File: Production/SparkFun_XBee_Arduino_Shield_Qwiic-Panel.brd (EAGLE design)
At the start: 120.9 x 213.4 mm, 1008 parts, among them J1 QWIIC_RIGHT_ANGLE, J13 QWIIC_RIGHT_ANGLE, J17 QWIIC_RIGHT_ANGLE, J21 QWIIC_RIGHT_ANGLE, J4 QWIIC_RIGHT_ANGLE, J9 QWIIC_RIGHT_ANGLE, Q1 220mA/50V/3.5Ω, Q11 3.1A/30V/105mΩ, Q12 220mA/50V/3.5Ω, Q13 20V/4.2A/52mΩ/1.4W, Q15 3.1A/30V/105mΩ, Q16 220mA/50V/3.5Ω, Q17 20V/4.2A/52mΩ/1.4W, Q19 3.1A/30V/105mΩ, Q2 20V/4.2A/52mΩ/1.4W, Q20 220mA/50V/3.5Ω, Q21 20V/4.2A/52mΩ/1.4W, Q23 3.1A/30V/105mΩ, Q24 220mA/50V/3.5Ω, Q3 3.1A/30V/105mΩ, Q5 20V/4.2A/52mΩ/1.4W, Q6 3.1A/30V/105mΩ, Q8 220mA/50V/3.5Ω, Q9 20V/4.2A/52mΩ/1.4W, U1 FSUSB30MUX_MSOP10, U10 FT231XS, U11 AP63203, U12 ESD Diode, U13 FSUSB30MUX_MSOP10, U14 ESD Diode, U15 FT231XS, U16 AP63203, U17 ESD Diode, U18 FSUSB30MUX_MSOP10, U19 ESD Diode, U2 AP63203, U20 FT231XS, U21 AP63203, U22 ESD Diode, U23 FSUSB30MUX_MSOP10, U24 ESD Diode, U25 FT231XS, U26 AP63203, U27 ESD Diode, U28 FSUSB30MUX_MSOP10, U29 ESD Diode, U3 ESD Diode, U30 FT231XS, U4 FT231XS, U5 ESD Diode, U6 AP63203, U7 ESD Diode, U8 FSUSB30MUX_MSOP10, U9 ESD Diode, X1 JUMPER-SMT_2_NO_SILK, X2 JUMPER-SMT_2_NO_SILK, X3 JUMPER-SMT_2_NO_SILK, X4 JUMPER-SMT_2_NO_SILK, X5 JUMPER-SMT_2_NO_SILK, X6 JUMPER-SMT_2_NO_SILK

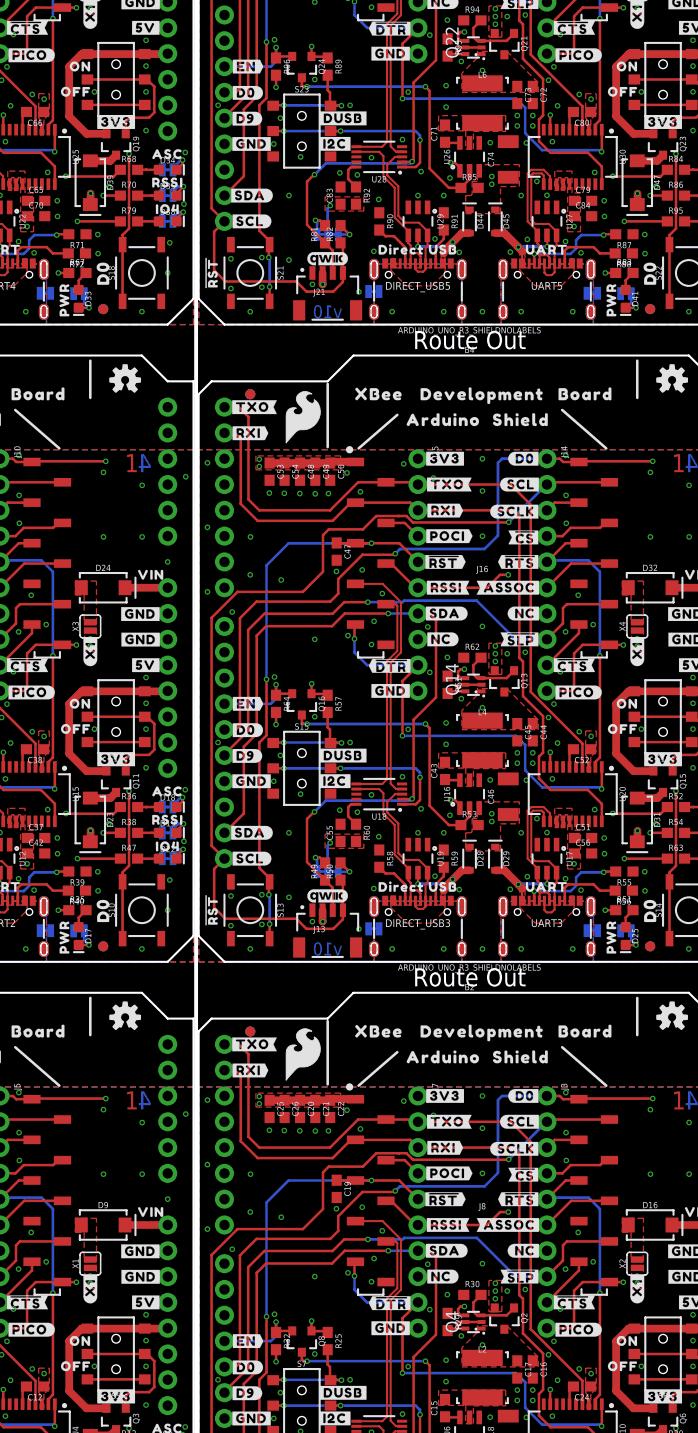
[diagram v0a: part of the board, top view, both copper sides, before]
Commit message: Adds Gerbers, updates ordering instructions to include material
* Fixes "Off" and "On" silk on switch
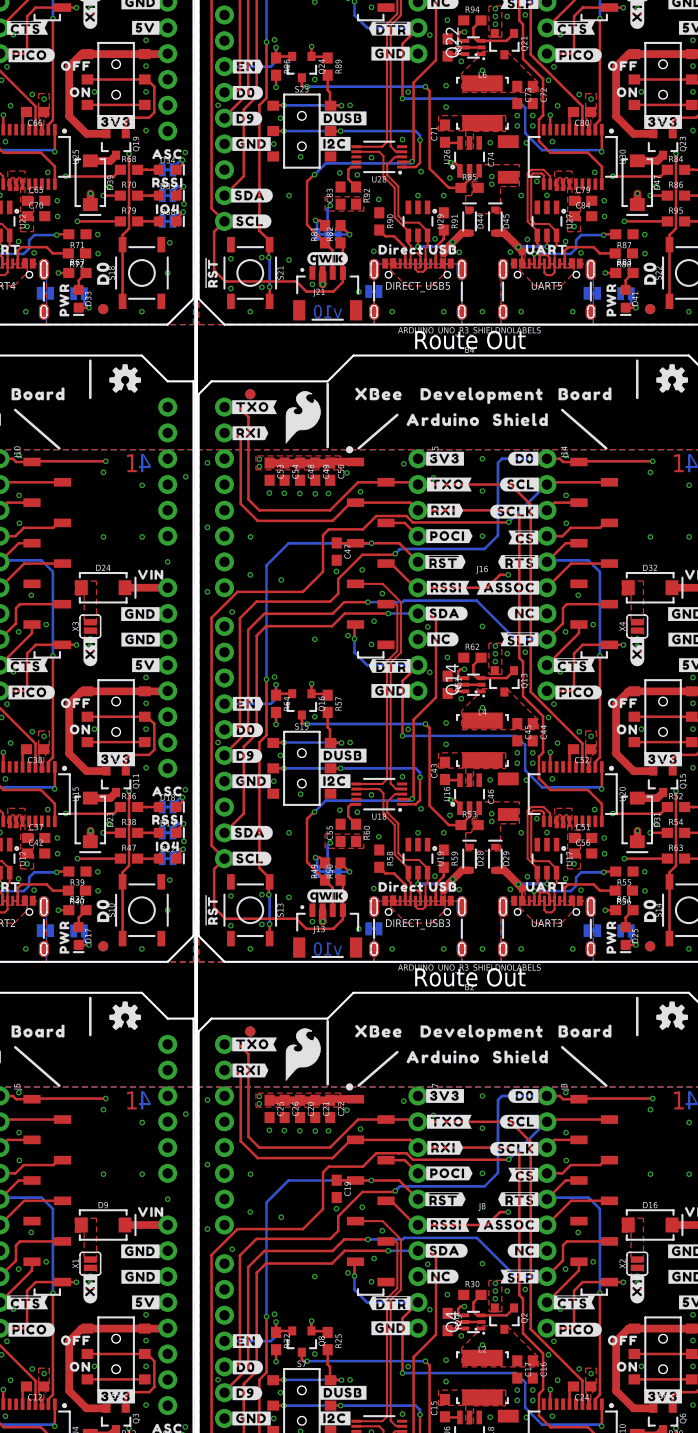
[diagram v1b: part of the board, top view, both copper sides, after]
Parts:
- moved U$255 2.54 mm to (41.8, 88.2)
- moved U$264 2.54 mm to (42.2, 85.6)
- moved U$347 2.54 mm to (95.6, 88.2)
- moved U$356 2.54 mm to (96.1, 85.6)
- moved U$163 2.54 mm to (95.6, 25.5)
- moved U$69 2.54 mm to (41.8, 25.5)
- moved U$172 2.54 mm to (96.1, 22.9)
- moved U$46 2.54 mm to (42.2, 22.9)
- moved U$439 2.54 mm to (41.8, 150.9)
- moved U$448 2.54 mm to (42.2, 148.3)
- moved U$531 2.54 mm to (95.6, 150.9)
- moved U$540 2.54 mm to (96.1, 148.3)
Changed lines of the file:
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@@
 <element name="U$41" library="topmirror" package="#GND#0" value="" x="48.1076" y="34.2392" smashed="yes"/>
 <element name="U$44" library="top" package="#3V3#1" value="" x="45.72" y="19.939" smashed="yes"/>
-<element name="U$69" library="pot" package="OFF311" value="" x="41.783" y="22.9108" smashed="yes"/>
+<element name="U$69" library="pot" package="OFF311" value="" x="41.783" y="25.4508" smashed="yes"/>
 <element name="U$52" library="top" package="#PLED#20" value="" x="45.5168" y="2.9972" smashed="yes" rot="MR0"/>
 <element name="U$93" library="pot" package="#IOLED#5" value="" x="47.0662" y="10.0584" smashed="yes" rot="MR0"/>
@@
 <element name="U$42" library="bot" package="#D0#3" value="" x="4.6736" y="22.8092" smashed="yes"/>
 <element name="U$43" library="bot" package="#X1#10" value="" x="43.18" y="30.6832" smashed="yes" rot="R90"/>
-<element name="U$46" library="bot" package="ON38" value="" x="42.2148" y="25.4" smashed="yes"/>
+<element name="U$46" library="bot" package="ON38" value="" x="42.2148" y="22.86" smashed="yes"/>
 <element name="U$53" library="topmirror" package="#GND#0" value="" x="48.1584" y="34.2392" smashed="yes" rot="MR0"/>
 <element name="U$63" library="topmirror" package="#GND#0" value="" x="48.133" y="31.7246" smashed="yes" rot="MR0"/>
@@
 <element name="U$161" library="topmirror" package="#GND#0" value="" x="101.9556" y="34.2392" smashed="yes"/>
 <element name="U$162" library="top" package="#3V3#1" value="" x="99.568" y="19.939" smashed="yes"/>
-<element name="U$163" library="pot" package="OFF311" value="" x="95.631" y="22.9108" smashed="yes"/>
+<element name="U$163" library="pot" package="OFF311" value="" x="95.631" y="25.4508" smashed="yes"/>
 <element name="U$164" library="top" package="#PLED#20" value="" x="99.3648" y="2.9972" smashed="yes" rot="MR0"/>
 <element name="U$165" library="pot" package="#IOLED#5" value="" x="100.9142" y="10.0584" smashed="yes" rot="MR0"/>
@@
 <element name="U$170" library="bot" package="#D0#3" value="" x="58.5216" y="22.8092" smashed="yes"/>
 <element name="U$171" library="bot" package="#X1#10" value="" x="97.028" y="30.6832" smashed="yes" rot="R90"/>
-<element name="U$172" library="bot" package="ON38" value="" x="96.0628" y="25.4" smashed="yes"/>
+<element name="U$172" library="bot" package="ON38" value="" x="96.0628" y="22.86" smashed="yes"/>
 <element name="U$173" library="topmirror" package="#GND#0" value="" x="102.0064" y="34.2392" smashed="yes" rot="MR0"/>
 <element name="U$174" library="topmirror" package="#GND#0" value="" x="101.981" y="31.7246" smashed="yes" rot="MR0"/>
@@
 <element name="U$253" library="topmirror" package="#GND#0" value="" x="48.1076" y="96.9772" smashed="yes"/>
 <element name="U$254" library="top" package="#3V3#1" value="" x="45.72" y="82.677" smashed="yes"/>
-<element name="U$255" library="pot" package="OFF311" value="" x="41.783" y="85.6488" smashed="yes"/>
+<element name="U$255" library="pot" package="OFF311" value="" x="41.783" y="88.1888" smashed="yes"/>
 <element name="U$256" library="top" package="#PLED#20" value="" x="45.5168" y="65.7352" smashed="yes" rot="MR0"/>
 <element name="U$257" library="pot" package="#IOLED#5" value="" x="47.0662" y="72.7964" smashed="yes" rot="MR0"/>
@@
 <element name="U$262" library="bot" package="#D0#3" value="" x="4.6736" y="85.5472" smashed="yes"/>
 <element name="U$263" library="bot" package="#X1#10" value="" x="43.18" y="93.4212" smashed="yes" rot="R90"/>
-<element name="U$264" library="bot" package="ON38" value="" x="42.2148" y="88.138" smashed="yes"/>
+<element name="U$264" library="bot" package="ON38" value="" x="42.2148" y="85.598" smashed="yes"/>
 <element name="U$265" library="topmirror" package="#GND#0" value="" x="48.1584" y="96.9772" smashed="yes" rot="MR0"/>
 <element name="U$266" library="topmirror" package="#GND#0" value="" x="48.133" y="94.4626" smashed="yes" rot="MR0"/>
@@
 <element name="U$345" library="topmirror" package="#GND#0" value="" x="101.9556" y="96.9772" smashed="yes"/>
 <element name="U$346" library="top" package="#3V3#1" value="" x="99.568" y="82.677" smashed="yes"/>
-<element name="U$347" library="pot" package="OFF311" value="" x="95.631" y="85.6488" smashed="yes"/>
+<element name="U$347" library="pot" package="OFF311" value="" x="95.631" y="88.1888" smashed="yes"/>
 <element name="U$348" library="top" package="#PLED#20" value="" x="99.3648" y="65.7352" smashed="yes" rot="MR0"/>
 <element name="U$349" library="pot" package="#IOLED#5" value="" x="100.9142" y="72.7964" smashed="yes" rot="MR0"/>
@@
 <element name="U$354" library="bot" package="#D0#3" value="" x="58.5216" y="85.5472" smashed="yes"/>
 <element name="U$355" library="bot" package="#X1#10" value="" x="97.028" y="93.4212" smashed="yes" rot="R90"/>
-<element name="U$356" library="bot" package="ON38" value="" x="96.0628" y="88.138" smashed="yes"/>
+<element name="U$356" library="bot" package="ON38" value="" x="96.0628" y="85.598" smashed="yes"/>
 <element name="U$357" library="topmirror" package="#GND#0" value="" x="102.0064" y="96.9772" smashed="yes" rot="MR0"/>
 <element name="U$358" library="topmirror" package="#GND#0" value="" x="101.981" y="94.4626" smashed="yes" rot="MR0"/>
@@
 <element name="U$437" library="topmirror" package="#GND#0" value="" x="48.1076" y="159.7152" smashed="yes"/>
 <element name="U$438" library="top" package="#3V3#1" value="" x="45.72" y="145.415" smashed="yes"/>
-<element name="U$439" library="pot" package="OFF311" value="" x="41.783" y="148.3868" smashed="yes"/>
+<element name="U$439" library="pot" package="OFF311" value="" x="41.783" y="150.9268" smashed="yes"/>
 <element name="U$440" library="top" package="#PLED#20" value="" x="45.5168" y="128.4732" smashed="yes" rot="MR0"/>
 <element name="U$441" library="pot" package="#IOLED#5" value="" x="47.0662" y="135.5344" smashed="yes" rot="MR0"/>
@@
 <element name="U$446" library="bot" package="#D0#3" value="" x="4.6736" y="148.2852" smashed="yes"/>
 <element name="U$447" library="bot" package="#X1#10" value="" x="43.18" y="156.1592" smashed="yes" rot="R90"/>
-<element name="U$448" library="bot" package="ON38" value="" x="42.2148" y="150.876" smashed="yes"/>
+<element name="U$448" library="bot" package="ON38" value="" x="42.2148" y="148.336" smashed="yes"/>
 <element name="U$449" library="topmirror" package="#GND#0" value="" x="48.1584" y="159.7152" smashed="yes" rot="MR0"/>
 <element name="U$450" library="topmirror" package="#GND#0" value="" x="48.133" y="157.2006" smashed="yes" rot="MR0"/>
@@
 <element name="U$529" library="topmirror" package="#GND#0" value="" x="101.9556" y="159.7152" smashed="yes"/>
 <element name="U$530" library="top" package="#3V3#1" value="" x="99.568" y="145.415" smashed="yes"/>
-<element name="U$531" library="pot" package="OFF311" value="" x="95.631" y="148.3868" smashed="yes"/>
+<element name="U$531" library="pot" package="OFF311" value="" x="95.631" y="150.9268" smashed="yes"/>
 <element name="U$532" library="top" package="#PLED#20" value="" x="99.3648" y="128.4732" smashed="yes" rot="MR0"/>
 <element name="U$533" library="pot" package="#IOLED#5" value="" x="100.9142" y="135.5344" smashed="yes" rot="MR0"/>
@@
 <element name="U$538" library="bot" package="#D0#3" value="" x="58.5216" y="148.2852" smashed="yes"/>
 <element name="U$539" library="bot" package="#X1#10" value="" x="97.028" y="156.1592" smashed="yes" rot="R90"/>
-<element name="U$540" library="bot" package="ON38" value="" x="96.0628" y="150.876" smashed="yes"/>
+<element name="U$540" library="bot" package="ON38" value="" x="96.0628" y="148.336" smashed="yes"/>
 <element name="U$541" library="topmirror" package="#GND#0" value="" x="102.0064" y="159.7152" smashed="yes" rot="MR0"/>
 <element name="U$542" library="topmirror" package="#GND#0" value="" x="101.981" y="157.2006" smashed="yes" rot="MR0"/>
